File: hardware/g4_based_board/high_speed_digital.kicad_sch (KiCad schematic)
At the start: 1 part, among them J9 Conn_01x05_Socket

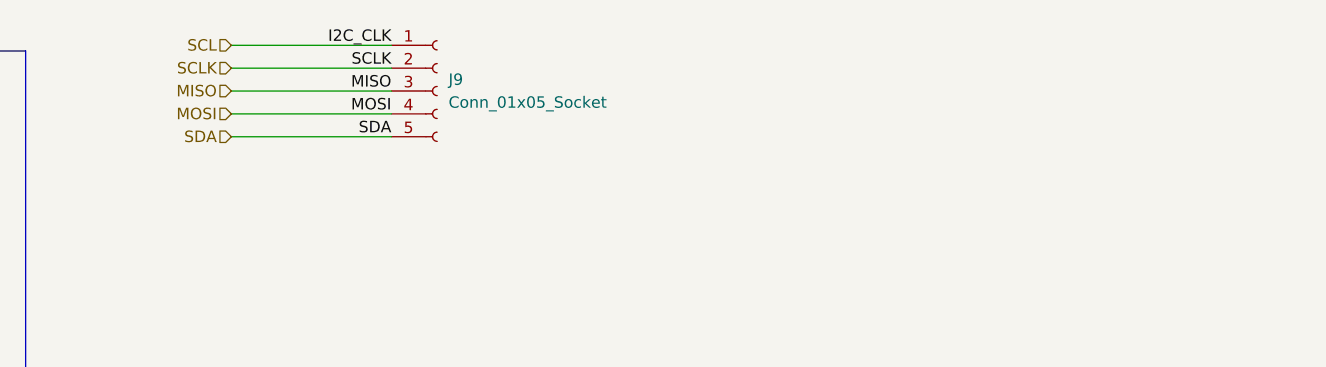
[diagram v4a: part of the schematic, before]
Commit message: changed headers to right layout
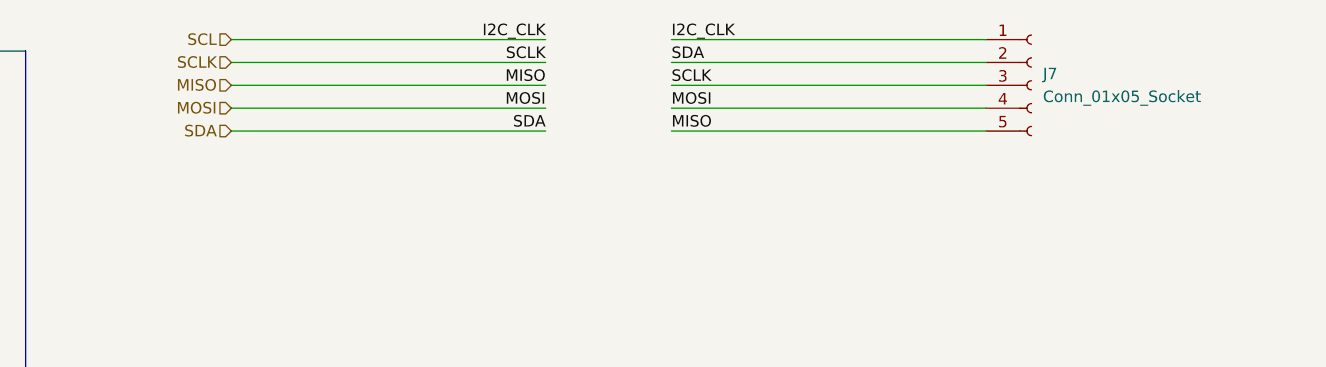
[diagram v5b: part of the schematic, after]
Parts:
- renumbered J9 to J7
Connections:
- net MISO: now also J7.5 (Pin_5); no longer J7.3 (Pin_3)
- net SCLK: now also J7.3 (Pin_3); no longer J7.2 (Pin_2)
- net SDA: now also J7.2 (Pin_2); no longer J7.5 (Pin_5)
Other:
- moved on the sheet: J7
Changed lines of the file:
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@@
+	(wire
+		(pts
+			(xy 69.215 18.415) (xy 104.14 18.415)
+		)
+		(stroke
+			(width 0)
+			(type default)
+		)
+	)
 	(wire
 		(pts
@@
 	(wire
 		(pts
+			(xy 69.215 28.575) (xy 104.14 28.575)
+		)
+		(stroke
+			(width 0)
+			(type default)
+		)
+	)
+	(wire
+		(pts
 			(xy 37.465 91.44) (xy 19.685 91.44)
 		)
@@
 	(wire
 		(pts
+			(xy 20.32 26.035) (xy 55.245 26.035)
+		)
+		(stroke
+			(width 0)
+			(type default)
+		)
+	)
+	(wire
+		(pts
 			(xy 37.465 127) (xy 19.685 127)
 		)
@@
 	(wire
 		(pts
-			(xy 20.32 24.13) (xy 38.1 24.13)
+			(xy 69.215 23.495) (xy 104.14 23.495)
+		)
+		(stroke
+			(width 0)
+			(type default)
+		)
+	)
+	(wire
+		(pts
+			(xy 69.215 26.035) (xy 104.14 26.035)
 		)
 		(stroke
@@
 	(wire
 		(pts
-			(xy 20.32 29.21) (xy 38.1 29.21)
+			(xy 20.32 18.415) (xy 55.245 18.415)
 		)
 		(stroke
@@
 	(wire
 		(pts
+			(xy 20.32 28.575) (xy 55.245 28.575)
+		)
+		(stroke
+			(width 0)
+			(type default)
+		)
+	)
+	(wire
+		(pts
 			(xy 37.465 154.94) (xy 29.845 154.94)
 		)
@@
 	(wire
 		(pts
+			(xy 20.32 20.955) (xy 55.245 20.955)
+		)
+		(stroke
+			(width 0)
+			(type default)
+		)
+	)
+	(wire
+		(pts
 			(xy 94.615 118.11) (xy 76.835 118.11)
 		)
@@
 	(wire
 		(pts
-			(xy 20.32 26.67) (xy 38.1 26.67)
-		)
-		(stroke
-			(width 0)
-			(type default)
-		)
-	)
-	(wire
-		(pts
-			(xy 20.32 19.05) (xy 38.1 19.05)
+			(xy 69.215 20.955) (xy 104.14 20.955)
+		)
+		(stroke
+			(width 0)
+			(type default)
+		)
+	)
+	(wire
+		(pts
+			(xy 20.32 23.495) (xy 55.245 23.495)
 		)
 		(stroke
@@
 		(pts
 			(xy 94.615 97.79) (xy 76.835 97.79)
-		)
-		(stroke
-			(width 0)
-			(type default)
-		)
-	)
-	(wire
-		(pts
-			(xy 20.32 21.59) (xy 38.1 21.59)
 		)
 		(stroke
@@
 		)
 	)
+	(label "SCLK"
+		(at 55.245 20.955 180)
+		(fields_autoplaced yes)
+		(effects
+			(font
+				(size 1.27 1.27)
+			)
+			(justify right bottom)
+		)
+	)
 	(label "EN_1"
 		(at 29.845 82.55 0)
@@
 		)
 	)
+	(label "MOSI"
+		(at 55.245 26.035 180)
+		(fields_autoplaced yes)
+		(effects
+			(font
+				(size 1.27 1.27)
+			)
+			(justify right bottom)
+		)
+	)
 	(label "SCLK"
 		(at 19.685 73.66 0)
@@
 		)
 	)
-	(label "SCLK"
-		(at 38.1 21.59 180)
-		(fields_autoplaced yes)
-		(effects
-			(font
-				(size 1.27 1.27)
-			)
-			(justify right bottom)
-		)
-	)
 	(label "MOSI"
 		(at 19.685 78.74 0)
@@
 		)
 	)
+	(label "MISO"
+		(at 69.215 28.575 0)
+		(fields_autoplaced yes)
+		(effects
+			(font
+				(size 1.27 1.27)
+			)
+			(justify left bottom)
+		)
+	)
 	(label "I2C_CLK"
 		(at 76.835 67.31 0)
@@
 	)
 	(label "I2C_CLK"
+		(at 55.245 18.415 180)
+		(fields_autoplaced yes)
+		(effects
+			(font
+				(size 1.27 1.27)
+			)
+			(justify right bottom)
+		)
+	)
+	(label "I2C_CLK"
 		(at 19.685 91.44 0)
 		(fields_autoplaced yes)
@@
 	)
 	(label "I2C_CLK"
-		(at 38.1 19.05 180)
-		(fields_autoplaced yes)
-		(effects
-			(font
-				(size 1.27 1.27)
-			)
-			(justify right bottom)
-		)
-	)
-	(label "I2C_CLK"
 		(at 19.685 115.57 0)
 		(fields_autoplaced yes)
@@
 		)
 	)
-	(label "SDA"
-		(at 38.1 29.21 180)
-		(fields_autoplaced yes)
-		(effects
-			(font
-				(size 1.27 1.27)
-			)
-			(justify right bottom)
-		)
-	)
 	(label "MOSI"
 		(at 76.835 102.87 0)
@@
 		)
 	)
-	(label "MOSI"
-		(at 38.1 26.67 180)
-		(fields_autoplaced yes)
-		(effects
-			(font
-				(size 1.27 1.27)
-			)
-			(justify right bottom)
-		)
-	)
 	(label "SCLK"
 		(at 19.685 121.92 0)
@@
 		)
 	)
+	(label "SDA"
+		(at 55.245 28.575 180)
+		(fields_autoplaced yes)
+		(effects
+			(font
+				(size 1.27 1.27)
+			)
+			(justify right bottom)
+		)
+	)
 	(label "MISO"
 		(at 19.685 148.59 0)
@@
 		)
 	)
+	(label "I2C_CLK"
+		(at 69.215 18.415 0)
+		(fields_autoplaced yes)
+		(effects
+			(font
+				(size 1.27 1.27)
+			)
+			(justify left bottom)
+		)
+	)
+	(label "MOSI"
+		(at 69.215 26.035 0)
+		(fields_autoplaced yes)
+		(effects
+			(font
+				(size 1.27 1.27)
+			)
+			(justify left bottom)
+		)
+	)
 	(label "SDA"
 		(at 76.835 93.98 0)
@@
 		)
 	)
-	(label "MISO"
-		(at 38.1 24.13 180)
-		(fields_autoplaced yes)
-		(effects
-			(font
-				(size 1.27 1.27)
-			)
-			(justify right bottom)
-		)
-	)
 	(label "I2C_CLK"
 		(at 76.835 91.44 0)
@@
 		)
 	)
+	(label "SDA"
+		(at 69.215 20.955 0)
+		(fields_autoplaced yes)
+		(effects
+			(font
+				(size 1.27 1.27)
+			)
+			(justify left bottom)
+		)
+	)
 	(label "MOSI"
 		(at 19.685 102.87 0)
@@
 		)
 	)
+	(label "MISO"
+		(at 55.245 23.495 180)
+		(fields_autoplaced yes)
+		(effects
+			(font
+				(size 1.27 1.27)
+			)
+			(justify right bottom)
+		)
+	)
 	(label "SDA"
 		(at 76.835 141.605 0)
@@
 	(label "SCLK"
 		(at 76.835 73.66 0)
+		(fields_autoplaced yes)
+		(effects
+			(font
+				(size 1.27 1.27)
+			)
+			(justify left bottom)
+		)
+	)
+	(label "SCLK"
+		(at 69.215 23.495 0)
 		(fields_autoplaced yes)
 		(effects
@@
 	(hierarchical_label "SDA"
 		(shape input)
-		(at 20.32 29.21 180)
+		(at 20.32 28.575 180)
 		(fields_autoplaced yes)
 		(effects
@@
 	(hierarchical_label "SCL"
 		(shape input)
-		(at 20.32 19.05 180)
+		(at 20.32 18.415 180)
 		(fields_autoplaced yes)
 		(effects
@@
 	(hierarchical_label "SCLK"
 		(shape input)
-		(at 20.32 21.59 180)
+		(at 20.32 20.955 180)
 		(fields_autoplaced yes)
 		(effects
@@
 	(hierarchical_label "MISO"
 		(shape input)
-		(at 20.32 24.13 180)
+		(at 20.32 23.495 180)
 		(fields_autoplaced yes)
 		(effects
@@
 	(hierarchical_label "MOSI"
 		(shape input)
-		(at 20.32 26.67 180)
+		(at 20.32 26.035 180)
 		(fields_autoplaced yes)
 		(effects
@@
 	(symbol
 		(lib_id "Connector:Conn_01x05_Socket")
-		(at 43.18 24.13 0)
+		(at 109.22 23.495 0)
 		(unit 1)
 		(exclude_from_sim no)
@@
 		(dnp no)
 		(fields_autoplaced yes)
-		(property "Reference" "J9"
-			(at 44.45 22.8599 0)
+		(property "Reference" "J7"
+			(at 110.49 22.2249 0)
 			(effects
 				(font
@@
 		)
 		(property "Value" "Conn_01x05_Socket"
-			(at 44.45 25.3999 0)
+			(at 110.49 24.7649 0)
 			(effects
 				(font
@@
 		)
 		(property "Footprint" "Connector_PinHeader_2.54mm:PinHeader_1x05_P2.54mm_Vertical"
-			(at 43.18 24.13 0)
+			(at 109.22 23.495 0)
 			(effects
 				(font
@@
 		)
 		(property "Datasheet" "~"
-			(at 43.18 24.13 0)
+			(at 109.22 23.495 0)
 			(effects
 				(font
@@
 		)
 		(property "Description" "Generic connector, single row, 01x05, script generated"
-			(at 43.18 24.13 0)
+			(at 109.22 23.495 0)
 			(effects
 				(font
@@
 			(project "data_logger"
 				(path "/9bc93932-ff5f-4f35-96cf-dfa5f042acb6/d4605b59-911a-47dc-8072-99de95361456"
-					(reference "J9")
+					(reference "J7")
 					(unit 1)
 				)

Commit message: rev-1
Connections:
- net MISO: now also J7.3 (Pin_3); no longer J7.5 (Pin_5)
- net SCLK: now also J7.5 (Pin_5); no longer J7.3 (Pin_3)
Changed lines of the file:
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@@
+	)
+	(label "MOSI"
+		(at 69.215 26.035 0)
+		(fields_autoplaced yes)
+		(effects
+			(font
+				(size 1.27 1.27)
+			)
+			(justify left bottom)
+		)
 	)
 	(label "MOSI"
@@
 	(label "MISO"
 		(at 19.685 124.46 0)
+		(fields_autoplaced yes)
+		(effects
+			(font
+				(size 1.27 1.27)
+			)
+			(justify left bottom)
+		)
+	)
+	(label "MISO"
+		(at 69.215 23.495 0)
 		(fields_autoplaced yes)
 		(effects
@@
 		)
 	)
+	(label "SCLK"
+		(at 69.215 28.575 0)
+		(fields_autoplaced yes)
+		(effects
+			(font
+				(size 1.27 1.27)
+			)
+			(justify left bottom)
+		)
+	)
 	(label "MOSI"
 		(at 76.835 78.74 0)
@@
 	(label "MOSI"
 		(at 19.685 78.74 0)
-		(fields_autoplaced yes)
-		(effects
-			(font
-				(size 1.27 1.27)
-			)
-			(justify left bottom)
-		)
-	)
-	(label "MISO"
-		(at 69.215 28.575 0)
 		(fields_autoplaced yes)
 		(effects
@@
 		)
 	)
-	(label "MOSI"
-		(at 69.215 26.035 0)
-		(fields_autoplaced yes)
-		(effects
-			(font
-				(size 1.27 1.27)
-			)
-			(justify left bottom)
-		)
-	)
 	(label "SDA"
 		(at 76.835 93.98 0)
@@
 		(fields_autoplaced yes)
 		(effects
-			(font
-				(size 1.27 1.27)
-			)
-			(justify left bottom)
-		)
-	)
-	(label "SCLK"
-		(at 69.215 23.495 0)
-		(fields_autoplaced yes)
-		(effects

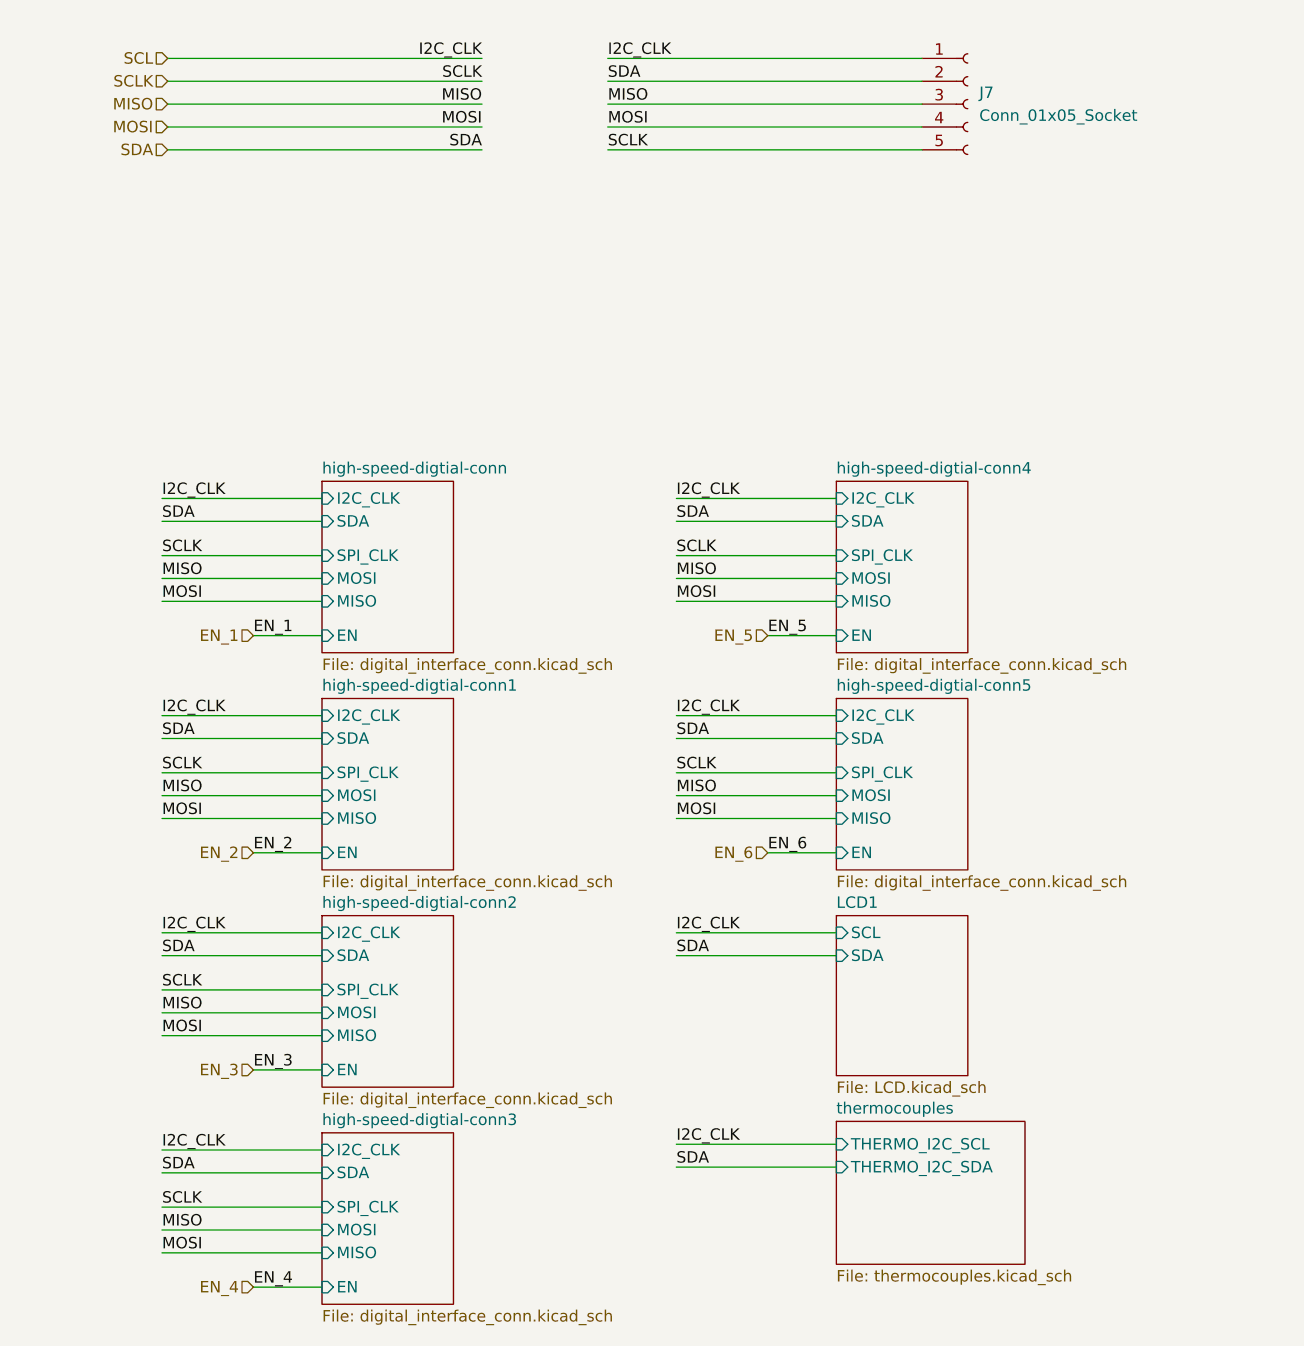
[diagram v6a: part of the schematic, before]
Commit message: minor addtion and swd header added and usart removed
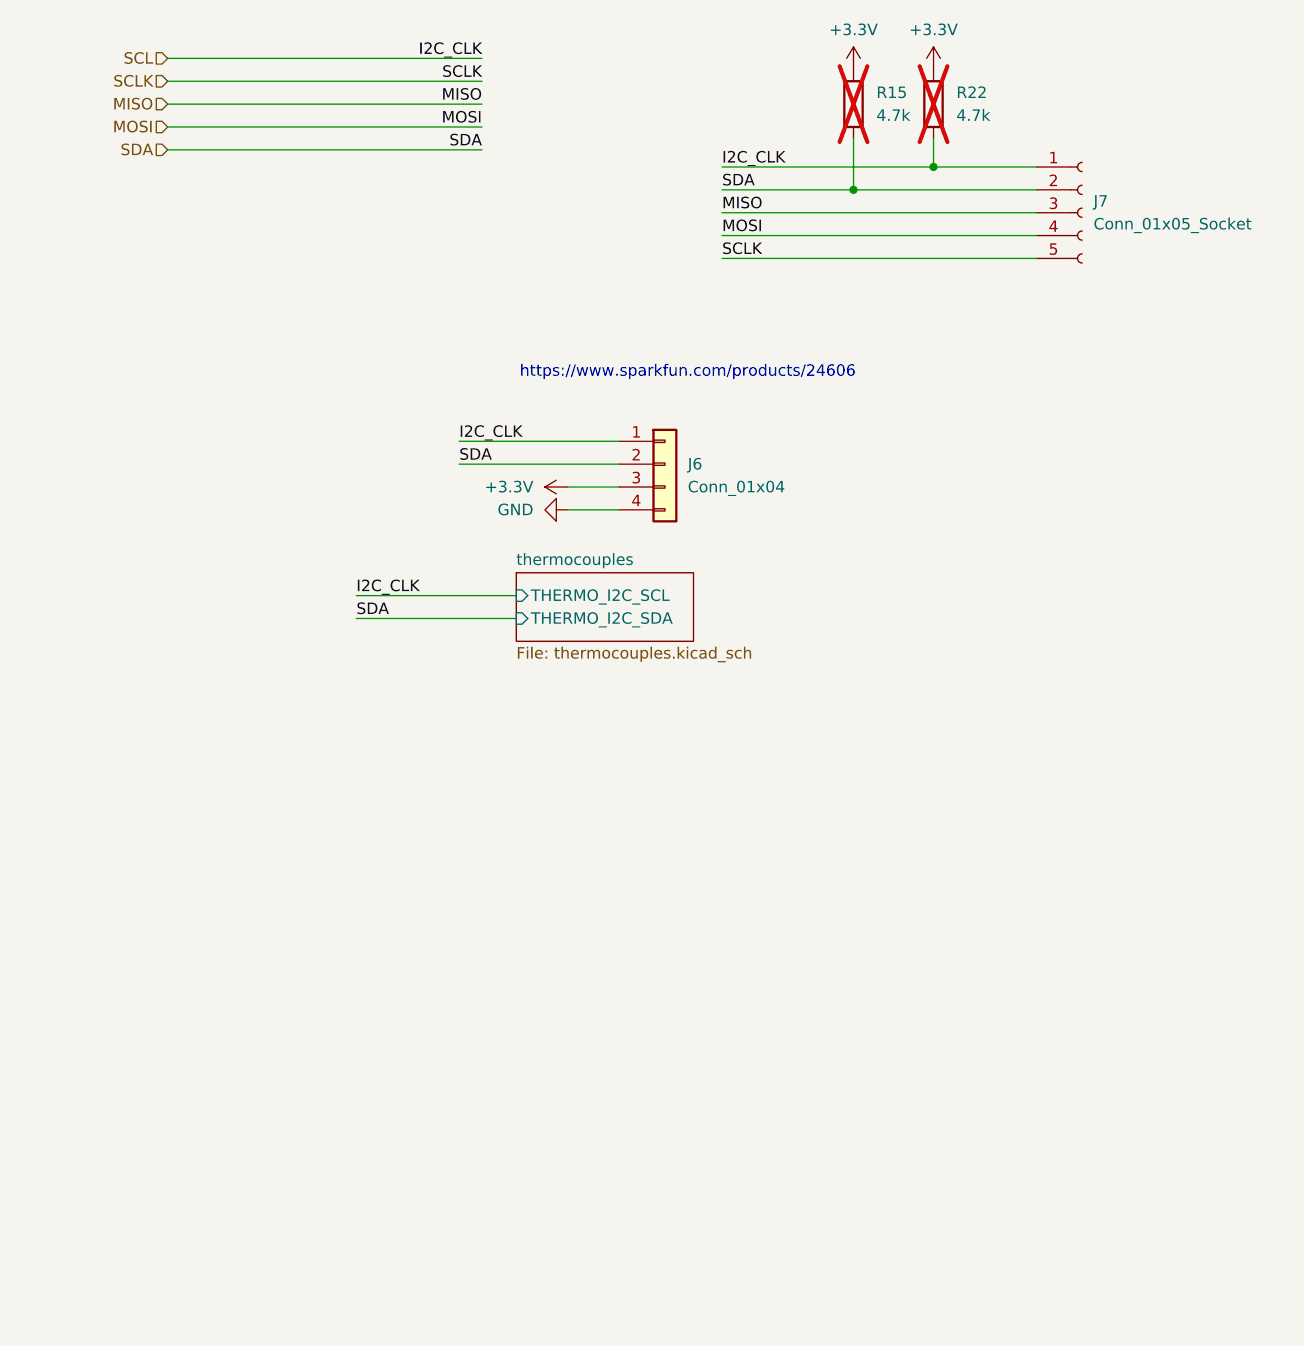
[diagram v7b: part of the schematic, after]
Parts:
- added J6: Conn_01x04, Connector_Molex:Molex_KK-254_AE-6410-04A_1x04_P2.54mm_Vertical, symbol Connector_Generic:Conn_01x04
- added R15, R22: 4.7k, Resistor_SMD:R_0603_1608Metric_Pad0.98x0.95mm_HandSolder, symbol Device:R
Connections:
- net SCL: now also J6.1 (Pin_1), R22.2
- net SDA: now also J6.2 (Pin_2), R15.2
- new net +3.3V: J6.3 (Pin_3), R15.1, R22.1
- new net GND: J6.4 (Pin_4)
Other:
- removed sheet LCD1
- removed sheet high-speed-digtial-conn
- removed sheet high-speed-digtial-conn1
- removed sheet high-speed-digtial-conn2
- removed sheet high-speed-digtial-conn3
- removed sheet high-speed-digtial-conn4
- removed sheet high-speed-digtial-conn5
- note added: "https://www.sparkfun.com/products/24606"
- moved on the sheet: J7
